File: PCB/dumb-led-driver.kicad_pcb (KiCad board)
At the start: 4 copper layers, 60 x 30 mm, 46 parts, among them J1 ProgConn-SOICBite, J2 12V PWR, Q1 UMW30N06, Q2 UMW30N06, Q3 UMW30N06, SW1 RESET, SW2 FLASH, U1 ESP-12F, U2 MCP1416, U4 MCP1416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

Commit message: added silkscreen to board and pictures to readme
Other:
- board text added: "IoT Dumb LED Strip Driver"
- board text added: "iot_pwm_leddriver jacobbokor.com v0.1 11-2023"
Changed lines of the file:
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@@
   (gr_arc (start 110 54) (mid 111.171573 51.171573) (end 114 50)
     (stroke (width 0.1) (type default)) (layer "Edge.Cuts"))
+  (gr_text "IoT Dumb LED\nStrip Driver" (at 123.7 63.1) (layer "B.SilkS" knockout)
+    (effects (font (size 2 2) (thickness 0.4) bold) (justify bottom mirror))
+  )
+  (gr_text "iot_pwm_leddriver\njacobbokor.com\nv0.1 11-2023" (at 122.9 54.9) (layer "B.SilkS")
+    (effects (font (size 1 1) (thickness 0.2) bold) (justify bottom mirror))
+  )
   (gr_text "12VDC\nMAX" (at 113.4 69.6) (layer "B.SilkS" knockout)
     (effects (font (size 1 1) (thickness 0.25) bold) (justify bottom mirror))

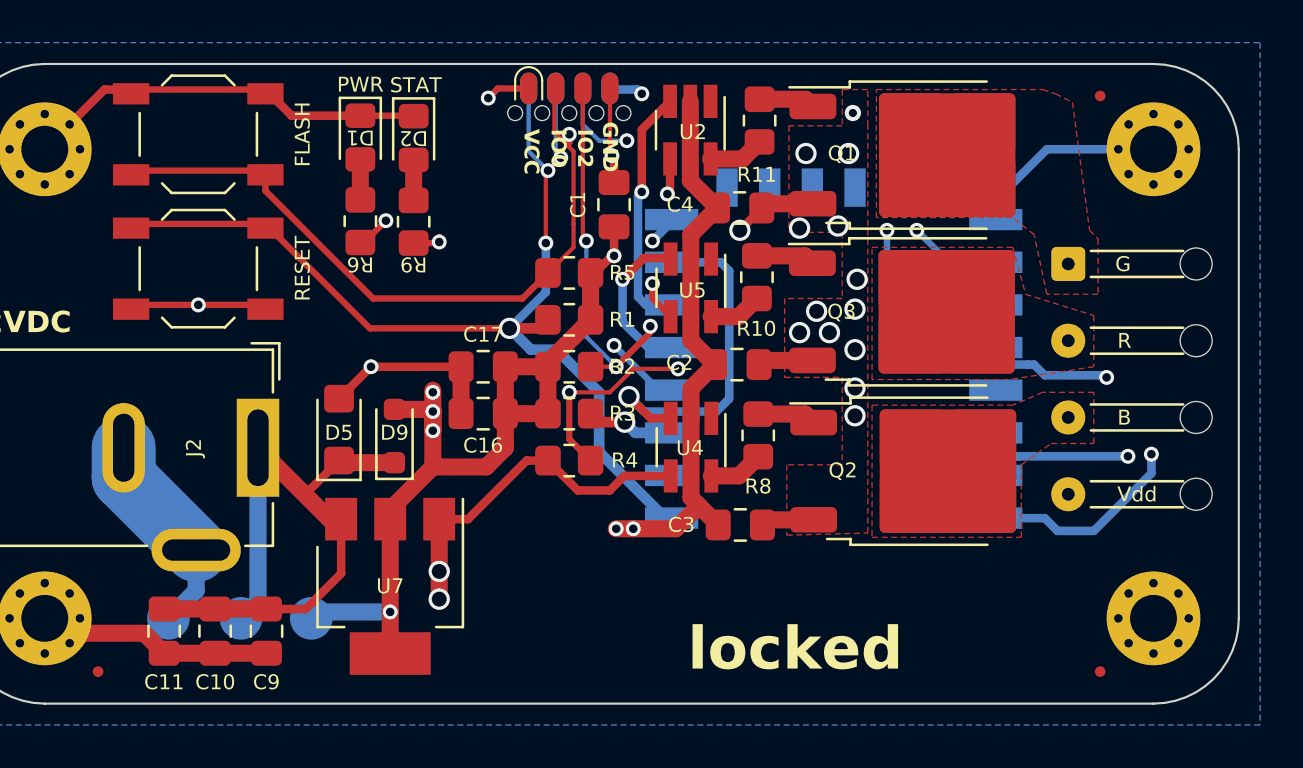
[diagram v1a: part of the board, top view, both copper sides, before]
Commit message: Redesign around new components added to scheamtic
 - shift left most of board
 - re-layout
 - new components
 - drc passes (mostly)
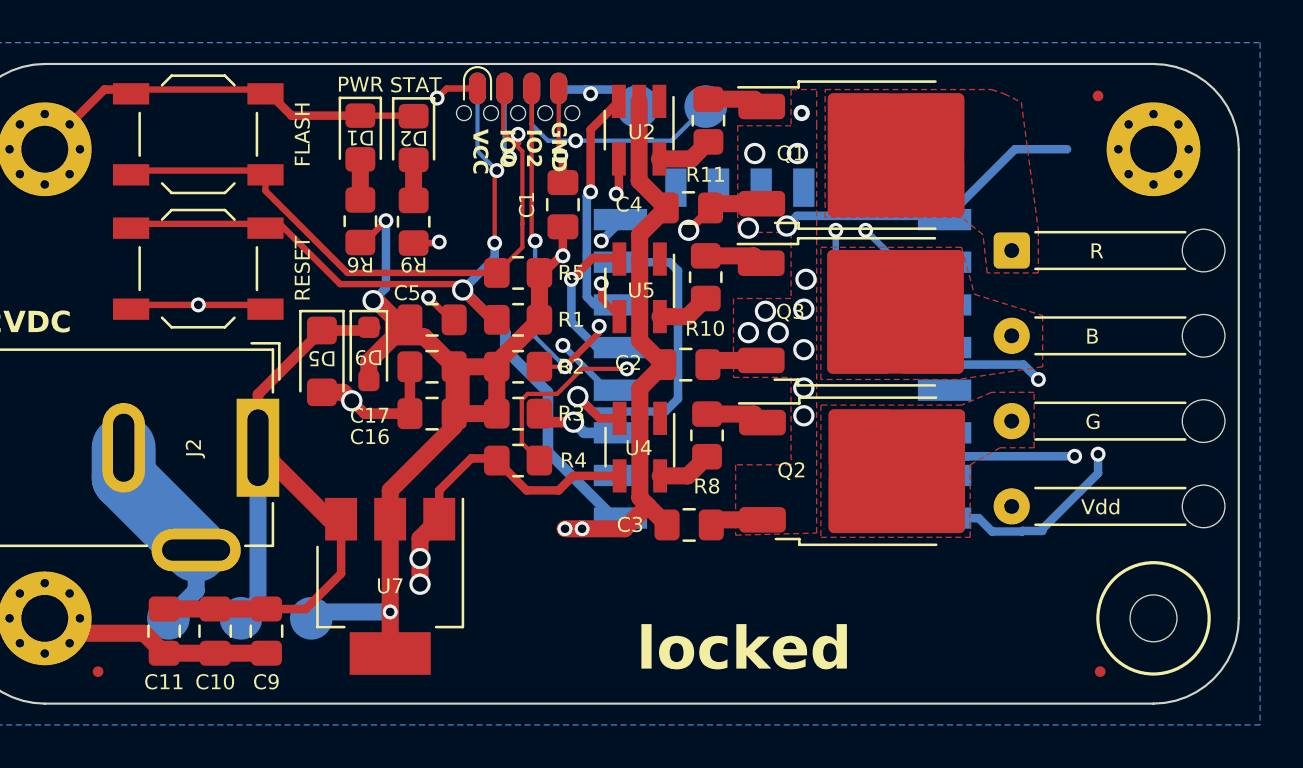
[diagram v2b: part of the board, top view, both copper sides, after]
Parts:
- added C5: 10uF, Capacitor_SMD:C_0805_2012Metric_Pad1.18x1.45mm_HandSolder, F.Cu at (132.2, 62.0)
- added TP4: RX, TestPoint:TestPoint_Pad_D2.0mm, B.Cu at (141.8, 52.0)
- added TP7: TX, TestPoint:TestPoint_Pad_D2.0mm, B.Cu at (145.0, 52.0)
- D3: footprint Connector_Wire:SolderWire-0.1sqmm_1x04_P3.6mm_D0.4mm_OD1mm_Relief -> Connector_Wire:SolderWire-0.15sqmm_1x04_P4mm_D0.5mm_OD1.5mm_Relief; moved to B.Cu
- H2: footprint MountingHole:MountingHole_2.2mm_M2_Pad_Via -> MountingHole:MountingHole_2.2mm_M2_ISO7380
- moved D3 11.8 mm to (159.3, 58.8), turned to -90 degrees
- moved D9 4.03 mm to (129.2, 63.6), turned to -90 degrees
- moved D5 3.30 mm to (127.0, 64.0), turned to -90 degrees
- moved C16 2.40 mm to (132.2, 66.4)
- moved C17 2.40 mm to (132.2, 64.2)
- moved C2 2.40 mm to (144.1, 64.1)
- moved C3 2.40 mm to (144.2, 71.6)
- moved C4 2.40 mm to (144.2, 56.8)
- moved J1 2.40 mm to (136.2, 50.4)
- moved Q1 2.40 mm to (152.7, 54.3)
- moved Q2 2.40 mm to (152.7, 69.1)
- moved Q3 2.40 mm to (152.6, 61.6)
- moved R1 2.40 mm to (136.2, 62.0)
- moved R10 2.40 mm to (145.0, 60.0)
- moved R11 2.40 mm to (145.1, 52.7)
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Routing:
- net VDD: track 99.9 -> 61.2 mm
- net /TX: track 44.1 -> 50.9 mm
- net +3.3V: track 48.8 -> 54.0 mm, vias 8 -> 6
- net Earth: track 96.3 -> 101.2 mm, vias 21 -> 22
- net /GPIO0: track 74.1 -> 69.9 mm
- net /~{RST}: track 47.0 -> 43.4 mm
- net /RX: track 45.7 -> 48.4 mm
- net Net-(U1-GPIO16): track 15.0 -> 12.5 mm
- net GPIO15: track 27.8 -> 27.3 mm, vias 3 -> 2
- added copper zone on In2.Cu, net VDD

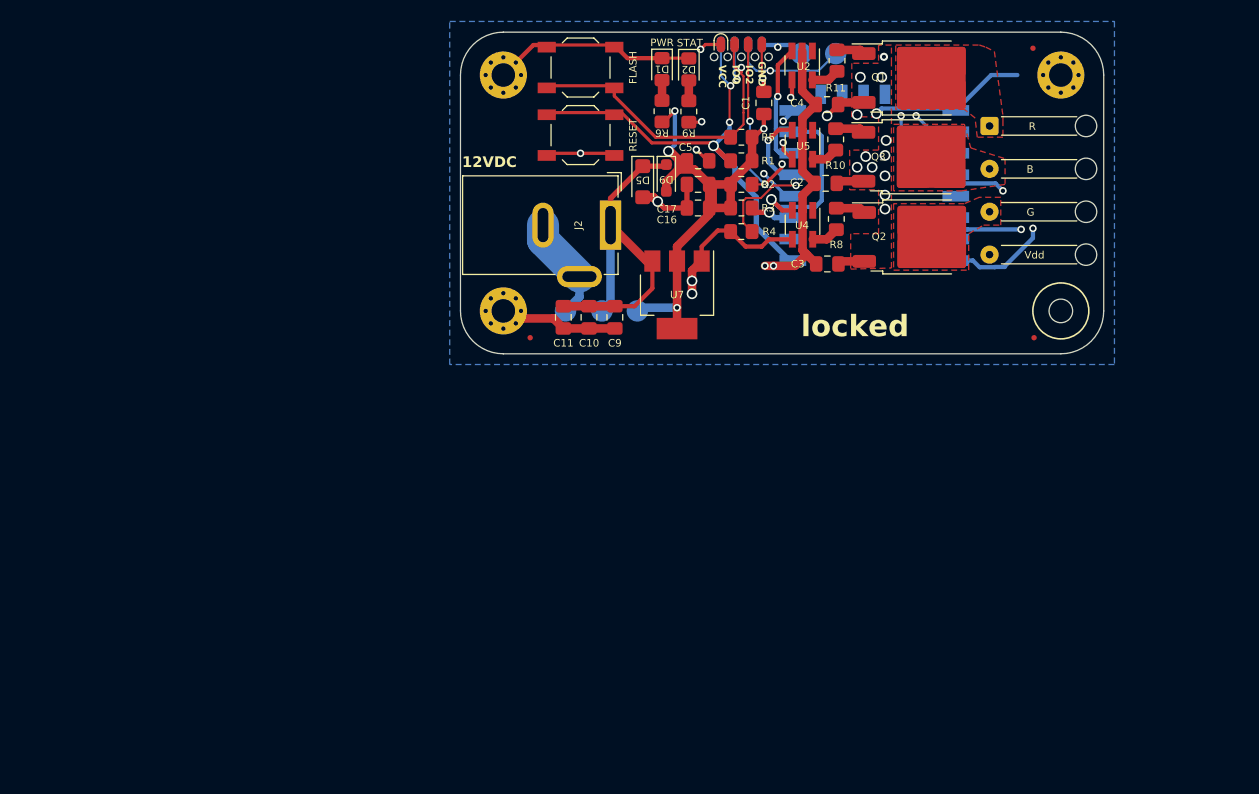
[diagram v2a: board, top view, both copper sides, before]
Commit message: fuse added to schematic. began board re-layout
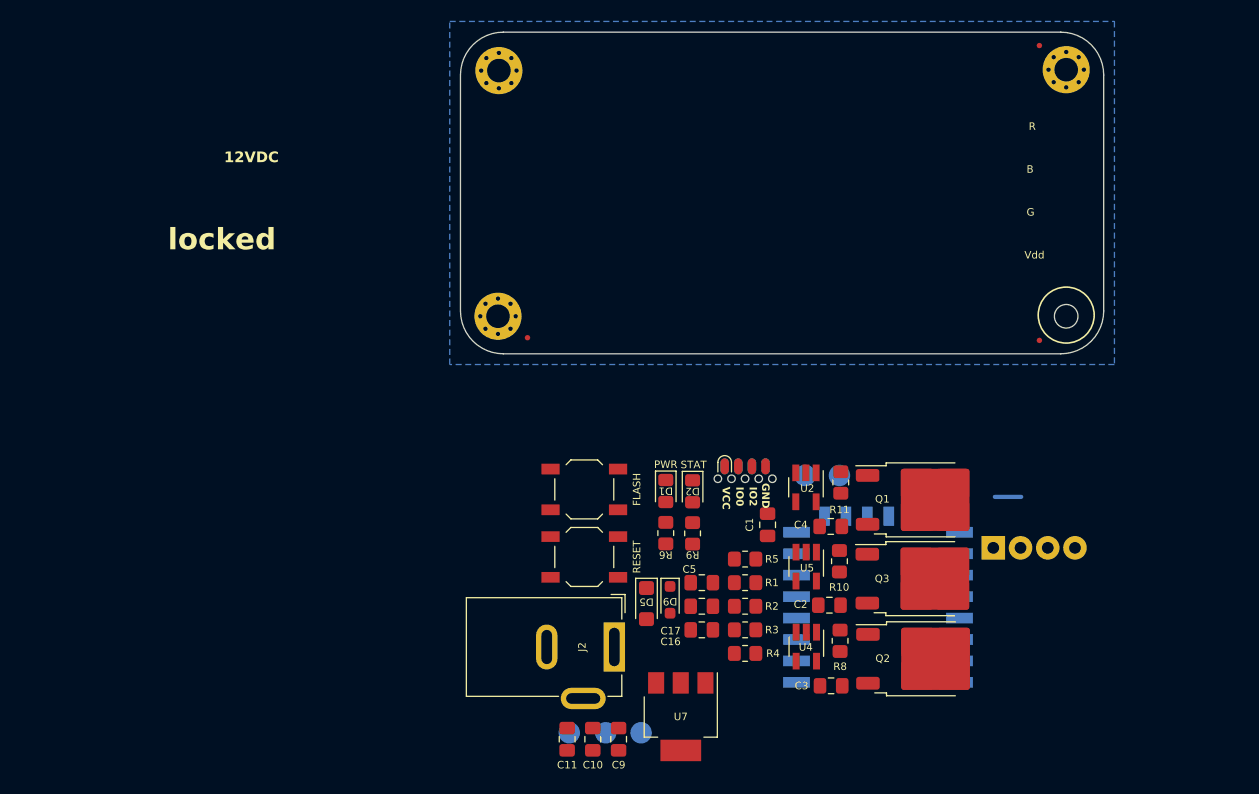
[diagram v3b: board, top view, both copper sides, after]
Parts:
- D3: footprint Connector_Wire:SolderWire-0.15sqmm_1x04_P4mm_D0.5mm_OD1.5mm_Relief -> TerminalBlock_Phoenix:TerminalBlock_Phoenix_MPT-0,5-4-2.54_1x04_P2.54mm_Horizontal
- moved Q2 39.4 mm to (153.1, 108.5)
- moved R4 39.4 mm to (136.6, 108.0)
- moved R5 39.4 mm to (136.6, 99.2)
- moved C10 39.4 mm to (122.3, 116.0)
- moved C11 39.4 mm to (120.0, 116.0)
- moved C2 39.4 mm to (144.4, 103.5)
- moved C9 39.4 mm to (124.8, 116.0)
- moved D9 39.4 mm to (129.6, 103.0)
- moved J1 39.4 mm to (136.6, 89.8)
- moved SW2 39.4 mm to (121.5, 92.7)
- moved U1 39.4 mm to (148.9, 107.2)
- moved C1 39.4 mm to (138.7, 96.0)
- moved C4 39.4 mm to (144.5, 96.1)
- moved D2 39.4 mm to (131.7, 92.8)
- moved Q1 39.4 mm to (153.0, 93.6)
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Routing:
- net Earth: track 101.2 -> 2.45 mm, vias 22 -> 0
- net /GPIO0: track 69.9 -> 0.00 mm, vias 2 -> 0
- net VDD: track 61.2 -> 0.00 mm, vias 2 -> 0
- net +3.3V: track 54.0 -> 0.00 mm, vias 6 -> 0
- net /TX: track 50.9 -> 0.00 mm, vias 2 -> 0
- net /RX: track 48.4 -> 0.00 mm, vias 2 -> 0
- net /~{RST}: track 43.4 -> 0.00 mm, vias 3 -> 0
- net GPIO2: track 38.0 -> 0.00 mm, vias 4 -> 0
- net GPIO15: track 27.3 -> 0.00 mm, vias 2 -> 0
- net EN: track 22.5 -> 0.00 mm, vias 2 -> 0
- net /LED Driver/LED_G: track 16.5 -> 0.00 mm, vias 1 -> 0
- net Net-(U1-GPIO16): track 12.5 -> 0.00 mm, vias 2 -> 0
- net /LED Driver/LED_R: track 11.5 -> 0.00 mm, vias 1 -> 0
- net /LED Driver/LED_B: track 7.48 -> 0.00 mm, vias 1 -> 0
- net /LED Driver/LED_G_G: track 2.77 -> 0.00 mm
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- removed copper zone on F.Cu, net /LED Driver/LED_B_GND
- removed copper zone on F.Cu, net /LED Driver/LED_G_GND
- removed copper zone on F.Cu, net /LED Driver/LED_R_GND
- removed copper zone on F.Cu, net Earth
- removed copper zone on In2.Cu, net VDD

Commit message: began rev2 of layout. board size will have to be increased
- will need to make compomises regarding I/O, wont be able to make both power in and out fit on same short side :(
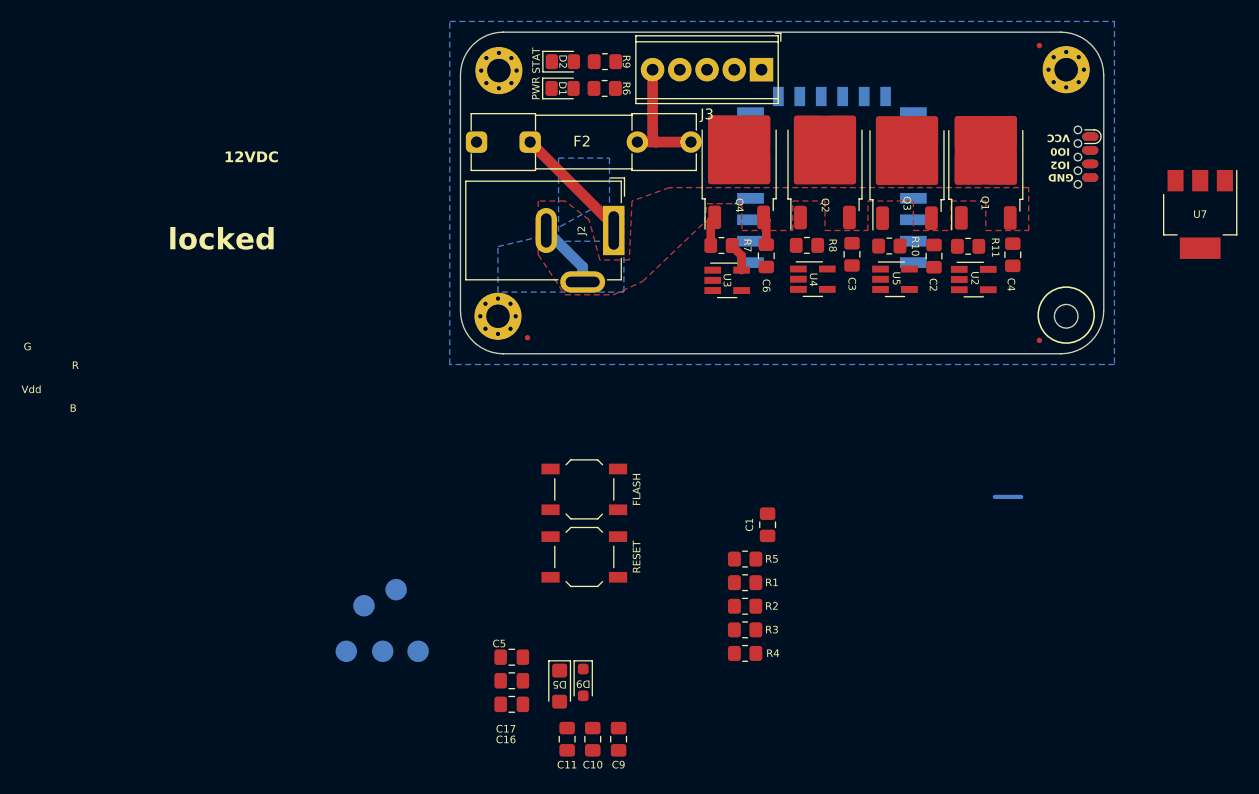
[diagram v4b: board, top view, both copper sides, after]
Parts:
- removed D3: LED_RBGA, TerminalBlock_Phoenix:TerminalBlock_Phoenix_MPT-0,5-4-2.54_1x04_P2.54mm_Horizontal
- added C6: 10uF, Capacitor_SMD:C_0805_2012Metric_Pad1.18x1.45mm_HandSolder, F.Cu at (138.5, 70.9)
- added F2: Fuse Holder, Fuse:Fuseholder_Clip-5x20mm_Littelfuse_111_Inline_P20.00x5.00mm_D1.05mm_Horizontal, F.Cu at (111.5, 60.2)
- added J3: LED_GRBWA, TerminalBlock_Phoenix:TerminalBlock_Phoenix_MPT-0,5-5-2.54_1x05_P2.54mm_Horizontal, F.Cu at (138.1, 53.5)
- added Q4: UMW30N06, Package_TO_SOT_SMD:TO-252-2, F.Cu at (136.0, 62.2)
- added R7: 100, Resistor_SMD:R_0805_2012Metric_Pad1.20x1.40mm_HandSolder, F.Cu at (134.3, 69.9)
- added U3: MCP1416, Package_TO_SOT_SMD:SOT-23-5_HandSoldering, F.Cu at (134.9, 73.2)
- H2: value MountingHole_Pad -> Non-via mounting hole
- moved U7 67.4 mm to (179.0, 67.0)
- moved Q2 47.1 mm to (144.0, 62.2), turned to 90 degrees
- moved R9 44.8 mm to (123.5, 52.8), turned to 0 degrees
- moved J1 43.3 mm to (169.5, 61.7), turned to 90 degrees
- moved TP4 42.9 mm to (101.0, 103.5), turned to 0 degrees
- moved TP7 42.7 mm to (104.0, 102.0), turned to 0 degrees
- moved R6 41.9 mm to (123.5, 55.2), turned to 0 degrees
- moved D2 41.9 mm to (119.5, 52.8), turned to 0 degrees
- moved C3 40.3 mm to (146.5, 70.7), turned to 90 degrees
- moved U1 39.4 mm to (144.7, 68.0)
- moved J2 38.9 mm to (124.3, 68.5)
- moved D1 38.8 mm to (119.5, 55.2), turned to 0 degrees
- moved Q3 38.7 mm to (151.7, 62.3), turned to 90 degrees
- moved R8 37.0 mm to (142.3, 69.9), turned to 180 degrees
- moved U4 34.3 mm to (142.9, 73.0), turned to 0 degrees
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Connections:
- J2 pad 1: VDD -> /12VDC IN
- U1 pad 20: unconnected-(U1-GPIO5-Pad20) -> /LED Driver/LED_W
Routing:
- net VDD: track 0.00 -> 11.9 mm
- net /12VDC IN: track 0.00 -> 11.5 mm
- net Earth: track 2.45 -> 8.86 mm
- net /LED Driver/LED_W_G: track 0.00 -> 2.78 mm
- net Net-(U3-OUT): track 0.00 -> 2.66 mm
- net /LED Driver/LED_G_GND: track 0.00 -> 2.45 mm
- added copper zone on B.Cu, net /12VDC IN
- added copper zone on F.Cu, net Earth
- added copper zone on B.Cu, net VDD
